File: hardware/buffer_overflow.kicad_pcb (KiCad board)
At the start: 2 copper layers, 33.1 x 29.9 mm, 20 parts, among them J1 E1, J2 E2, U1 LM741

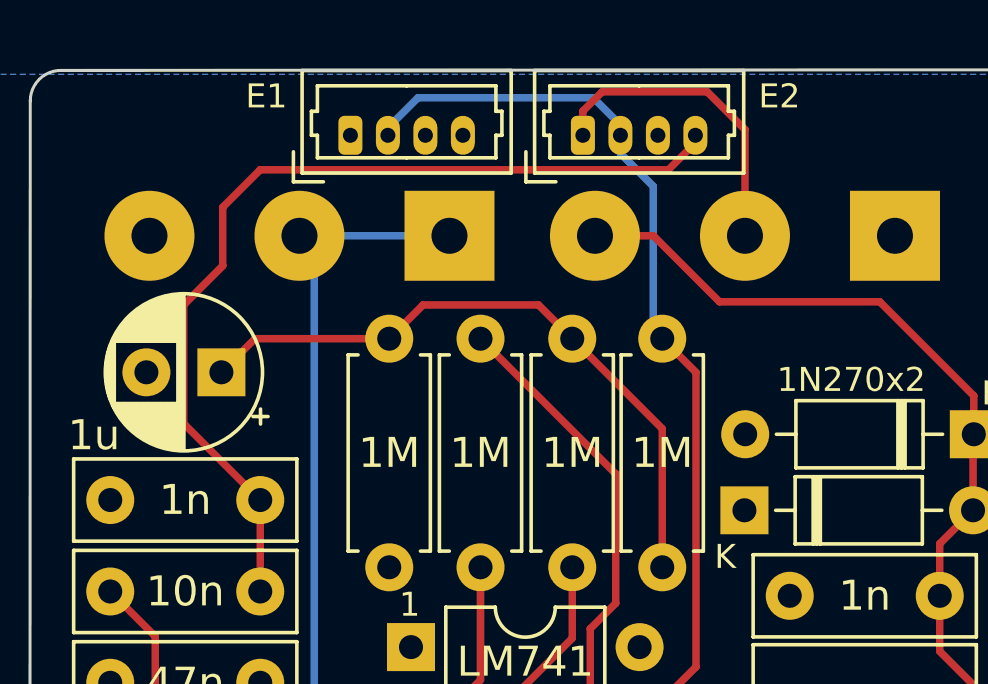
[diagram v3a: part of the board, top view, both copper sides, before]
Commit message: swap connectors to be on the same side as Noise Floor
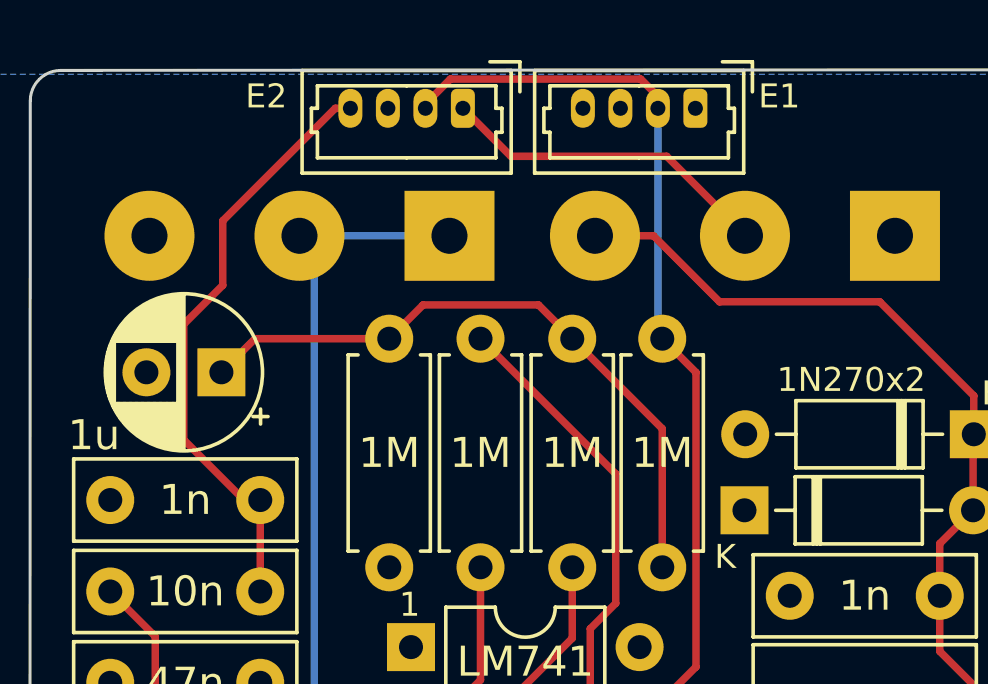
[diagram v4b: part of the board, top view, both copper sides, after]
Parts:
- moved J1 11.5 mm to (67.3, 29.2), turned to 180 degrees
- moved J2 4.10 mm to (59.6, 29.2), turned to 180 degrees
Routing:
- net /EFFECT_IN: track 31.3 -> 20.1 mm
- net /EFFECT_OUT: track 10.5 -> 11.2 mm
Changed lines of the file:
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@@
     (title "Buffer Overflow Drive Effect")
     (date "2023-03-03")
-    (rev "v0.36")
+    (rev "v0.37")
     (comment 1 " github.com/whbeers/buffer_overflow")
   )
@@
   )
   (footprint "Connector_Molex:Molex_PicoBlade_53047-0410_1x04_P1.25mm_Vertical" (layer "F.Cu")
-    (at 55.805112 30.1)
+    (at 67.305113 29.199999 180)
     (descr "Molex PicoBlade Connector System, 53047-0410, 4 Pins per row (http://www.molex.com/pdm_docs/sd/530470610_sd.pdf), generated with kicad-footprint-generator")
     (tags "connector Molex PicoBlade side entry")
@@
         (effects (font (size 1 1) (thickness 0.15)))
     )
-    (fp_text value "E1" (at -2.8 -1.3) (layer "F.SilkS" knockout)
+    (fp_text value "E1" (at -2.794887 0.399999) (layer "F.SilkS" knockout)
         (effects (font (size 0.8 0.8) (thickness 0.15)))
     )
@@
     (fp_line (start 5.25 1.15) (end 5.25 -2.05)
       (stroke (width 0.1) (type solid)) (layer "F.Fab"))
-    (pad "1" thru_hole roundrect (at 0 0) (size 0.8 1.3) (drill 0.5) (layers "*.Cu" "*.Mask") (roundrect_rratio 0.25)
+    (pad "1" thru_hole roundrect (at 0 0 180) (size 0.8 1.3) (drill 0.5) (layers "*.Cu" "*.Mask") (roundrect_rratio 0.25)
       (net 12 "unconnected-(J1-Pin_1-Pad1)") (pinfunction "Pin_1") (pintype "passive+no_connect"))
-    (pad "2" thru_hole oval (at 1.25 0) (size 0.8 1.3) (drill 0.5) (layers "*.Cu" "*.Mask")
+    (pad "2" thru_hole oval (at 1.25 0 180) (size 0.8 1.3) (drill 0.5) (layers "*.Cu" "*.Mask")
       (net 13 "/9V0") (pinfunction "Pin_2") (pintype "passive"))
-    (pad "3" thru_hole oval (at 2.5 0) (size 0.8 1.3) (drill 0.5) (layers "*.Cu" "*.Mask")
+    (pad "3" thru_hole oval (at 2.5 0 180) (size 0.8 1.3) (drill 0.5) (layers "*.Cu" "*.Mask")
       (net 14 "unconnected-(J1-Pin_3-Pad3)") (pinfunction "Pin_3") (pintype "passive+no_connect"))
-    (pad "4" thru_hole oval (at 3.75 0) (size 0.8 1.3) (drill 0.5) (layers "*.Cu" "*.Mask")
+    (pad "4" thru_hole oval (at 3.75 0 180) (size 0.8 1.3) (drill 0.5) (layers "*.Cu" "*.Mask")
       (net 15 "unconnected-(J1-Pin_4-Pad4)") (pinfunction "Pin_4") (pintype "passive+no_connect"))
     (model "${KICAD6_3DMODEL_DIR}/Connector_Molex.3dshapes/Molex_PicoBlade_53047-0410_1x04_P1.25mm_Vertical.wrl"
@@
   )
   (footprint "Connector_Molex:Molex_PicoBlade_53047-0410_1x04_P1.25mm_Vertical" (layer "F.Cu")
-    (at 63.555112 30.1)
+    (at 59.555113 29.199999 180)
     (descr "Molex PicoBlade Connector System, 53047-0410, 4 Pins per row (http://www.molex.com/pdm_docs/sd/530470610_sd.pdf), generated with kicad-footprint-generator")
     (tags "connector Molex PicoBlade side entry")
@@
         (effects (font (size 1 1) (thickness 0.15)))
     )
-    (fp_text value "E2" (at 6.55 -1.3) (layer "F.SilkS" knockout)
+    (fp_text value "E2" (at 6.555113 0.399999) (layer "F.SilkS" knockout)
         (effects (font (size 0.8 0.8) (thickness 0.15)))
     )
@@
     (fp_line (start 5.25 1.15) (end 5.25 -2.05)
       (stroke (width 0.1) (type solid)) (layer "F.Fab"))
-    (pad "1" thru_hole roundrect (at 0 0) (size 0.8 1.3) (drill 0.5) (layers "*.Cu" "*.Mask") (roundrect_rratio 0.25)
+    (pad "1" thru_hole roundrect (at 0 0 180) (size 0.8 1.3) (drill 0.5) (layers "*.Cu" "*.Mask") (roundrect_rratio 0.25)
       (net 16 "/EFFECT_OUT") (pinfunction "Pin_1") (pintype "passive"))
-    (pad "2" thru_hole oval (at 1.25 0) (size 0.8 1.3) (drill 0.5) (layers "*.Cu" "*.Mask")
+    (pad "2" thru_hole oval (at 1.25 0 180) (size 0.8 1.3) (drill 0.5) (layers "*.Cu" "*.Mask")
       (net 13 "/9V0") (pinfunction "Pin_2") (pintype "passive"))
-    (pad "3" thru_hole oval (at 2.5 0) (size 0.8 1.3) (drill 0.5) (layers "*.Cu" "*.Mask")
+    (pad "3" thru_hole oval (at 2.5 0 180) (size 0.8 1.3) (drill 0.5) (layers "*.Cu" "*.Mask")
       (net 1 "GND") (pinfunction "Pin_3") (pintype "passive"))
-    (pad "4" thru_hole oval (at 3.75 0) (size 0.8 1.3) (drill 0.5) (layers "*.Cu" "*.Mask")
+    (pad "4" thru_hole oval (at 3.75 0 180) (size 0.8 1.3) (drill 0.5) (layers "*.Cu" "*.Mask")
       (net 5 "/EFFECT_IN") (pinfunction "Pin_4") (pintype "passive"))
     (model "${KICAD6_3DMODEL_DIR}/Connector_Molex.3dshapes/Molex_PicoBlade_53047-0410_1x04_P1.25mm_Vertical.wrl"
@@
   (segment (start 70.95 54.45) (end 75.45 49.95) (width 0.25) (layer "F.Cu") (net 4))
   (segment (start 68.99 54.45) (end 70.95 54.45) (width 0.25) (layer "F.Cu") (net 4))
-  (segment (start 67.305112 30.35) (end 66.405112 31.25) (width 0.25) (layer "F.Cu") (net 5))
-  (segment (start 52.8 31.25) (end 51.55 32.5) (width 0.25) (layer "F.Cu") (net 5))
-  (segment (start 50.25 39.708) (end 52.8 42.258) (width 0.25) (layer "F.Cu") (net 5))
+  (segment (start 51.55 32.95) (end 51.55 35.1) (width 0.25) (layer "F.Cu") (net 5))
+  (segment (start 50.25 36.4) (end 50.25 40.25) (width 0.25) (layer "F.Cu") (net 5))
+  (segment (start 55.805113 29.199999) (end 55.300001 29.199999) (width 0.25) (layer "F.Cu") (net 5))
   (segment (start 52.8 42.258) (end 52.8 45.306) (width 0.25) (layer "F.Cu") (net 5))
-  (segment (start 66.405112 31.25) (end 52.8 31.25) (width 0.25) (layer "F.Cu") (net 5))
-  (segment (start 51.55 34.45) (end 50.25 35.75) (width 0.25) (layer "F.Cu") (net 5))
-  (segment (start 51.55 32.5) (end 51.55 34.45) (width 0.25) (layer "F.Cu") (net 5))
-  (segment (start 50.25 35.75) (end 50.25 39.708) (width 0.25) (layer "F.Cu") (net 5))
-  (segment (start 67.305112 30.1) (end 67.305112 30.35) (width 0.25) (layer "F.Cu") (net 5))
+  (segment (start 51.55 35.1) (end 50.25 36.4) (width 0.25) (layer "F.Cu") (net 5))
+  (segment (start 55.300001 29.199999) (end 51.55 32.95) (width 0.25) (layer "F.Cu") (net 5))
+  (segment (start 50.25 40.25) (end 52.258 42.258) (width 0.25) (layer "F.Cu") (net 5))
+  (segment (start 52.258 42.258) (end 52.8 42.258) (width 0.25) (layer "F.Cu") (net 5))
   (segment (start 46.69 54.448) (end 49.3 51.838) (width 0.25) (layer "F.Cu") (net 6))
   (segment (start 49.3 51.838) (end 49.3 46.806) (width 0.25) (layer "F.Cu") (net 6))
@@
   (segment (start 67.325 38.005) (end 67.325 47.82) (width 0.25) (layer "F.Cu") (net 13))
   (segment (start 67.325 47.82) (end 65.445 49.7) (width 0.25) (layer "F.Cu") (net 13))
+  (segment (start 66.055113 28.799999) (end 65.480113 28.224999) (width 0.25) (layer "F.Cu") (net 13))
+  (segment (start 65.480113 28.224999) (end 59.137651 28.224999) (width 0.25) (layer "F.Cu") (net 13))
+  (segment (start 66.055113 29.199999) (end 66.055113 28.799999) (width 0.25) (layer "F.Cu") (net 13))
+  (segment (start 59.137651 28.224999) (end 58.305113 29.057537) (width 0.25) (layer "F.Cu") (net 13))
+  (segment (start 58.305113 29.057537) (end 58.305113 29.199999) (width 0.25) (layer "F.Cu") (net 13))
   (segment (start 66.2 36.88) (end 67.325 38.005) (width 0.25) (layer "F.Cu") (net 13))
-  (segment (start 58.055112 28.85) (end 57.055112 29.85) (width 0.25) (layer "B.Cu") (net 13))
-  (segment (start 64.805112 30.1) (end 64.805112 29.755112) (width 0.25) (layer "B.Cu") (net 13))
-  (segment (start 64.805112 29.755112) (end 63.9 28.85) (width 0.25) (layer "B.Cu") (net 13))
-  (segment (start 57.05 30.3) (end 57.05 29.8) (width 0.25) (layer "B.Cu") (net 13))
-  (segment (start 65.9 31.8) (end 64.805112 30.705112) (width 0.25) (layer "B.Cu") (net 13))
-  (segment (start 65.9 36.58) (end 65.9 31.8) (width 0.25) (layer "B.Cu") (net 13))
-  (segment (start 66.2 36.88) (end 65.9 36.58) (width 0.25) (layer "B.Cu") (net 13))
-  (segment (start 57.055112 29.85) (end 57.055112 30.1) (width 0.25) (layer "B.Cu") (net 13))
-  (segment (start 63.9 28.85) (end 58.055112 28.85) (width 0.25) (layer "B.Cu") (net 13))
-  (segment (start 64.805112 30.705112) (end 64.805112 30.1) (width 0.25) (layer "B.Cu") (net 13))
-  (segment (start 63.555112 29.294888) (end 63.555112 30.1) (width 0.25) (layer "F.Cu") (net 16))
-  (segment (start 68.9575 29.9075) (end 67.7 28.65) (width 0.25) (layer "F.Cu") (net 16))
-  (segment (start 68.9575 33.45) (end 68.9575 29.9075) (width 0.25) (layer "F.Cu") (net 16))
-  (segment (start 64.2 28.65) (end 63.555112 29.294888) (width 0.25) (layer "F.Cu") (net 16))
-  (segment (start 67.7 28.65) (end 64.2 28.65) (width 0.25) (layer "F.Cu") (net 16))
+  (segment (start 66.055113 29.199999) (end 66.055113 36.735113) (width 0.25) (layer "B.Cu") (net 13))
+  (segment (start 66.055113 36.735113) (end 66.2 36.88) (width 0.25) (layer "B.Cu") (net 13))
+  (segment (start 61.155114 30.8) (end 59.555113 29.199999) (width 0.25) (layer "F.Cu") (net 16))
+  (segment (start 66.35 30.8) (end 61.155114 30.8) (width 0.25) (layer "F.Cu") (net 16))
+  (segment (start 68.9575 33.45) (end 68.9575 33.4075) (width 0.25) (layer "F.Cu") (net 16))
+  (segment (start 68.9575 33.4075) (end 66.35 30.8) (width 0.25) (layer "F.Cu") (net 16))
   (zone (net 1) (net_name "GND") (layer "B.Cu") (hatch edge 0.5)
     (connect_pads yes (clearance 0.508))
@@
         (xy 42.545 28.067)
       )
-    )
-  )
-  (group "" (id 44640d10-d8b0-4d10-8120-2862c2ace293)
-    (members
-      2863f98b-8943-4d5b-a6a4-d4917c9955a0
-      e8f1f366-1300-4382-9eb1-e7ea8b674607
     )
   )
@@
     (members
       e10283d1-a943-448b-b704-b4369c76185f
-      e59c07ca-e828-485d-8df7-598f3e4653e9
     )
   )
@@
     )
   )
+  (group "" (id 44640d10-d8b0-4d10-8120-2862c2ace293)
+    (members
+      2863f98b-8943-4d5b-a6a4-d4917c9955a0
+      3fd1133f-6a15-453f-9955-076d7ddada48
+      58ac90e8-e3b5-4925-9eaf-6aa123984e52
+      695f64c0-f4cf-4480-8a71-49eea9fb64d9
+      a26313fd-cb98-48cc-a445-f2466f3eeba6
+      af7734d1-66ab-49d0-ae24-1201dfe3ad5b
+      beb3796a-b8f2-4311-8699-af5658786aba
+      bf1f60d0-b900-4a9c-ae57-c94d054c15dd
+      d71d6460-fbc3-441c-965b-82b468e7d0f1
+      e8f1f366-1300-4382-9eb1-e7ea8b674607
+      e989a740-62a0-4e95-a4c7-73adee2570a0
+      eab2ae7c-9b4e-4f0e-9e92-98b32670b376
+      fd5ebd50-ebef-48b8-9dc5-55969baaa9df
+    )
+  )

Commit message: condense to a single connector, bump rev to v0.38
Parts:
- removed the J1 at (67.3, 29.2)
- J1: renamed from J2; value E2 -> E1
- moved J1 3.82 mm to (63.4, 29.2)
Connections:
- net VREF renamed /VREF
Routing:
- net /9V0: track 30.7 -> 24.7 mm
- net /EFFECT_OUT: track 11.2 -> 7.32 mm
- net /EFFECT_IN: track 20.1 -> 23.9 mm
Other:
- board size 33.1 x 29.9 mm -> 33.1 x 30.1 mm
- board text added: "${COMMENT1} ${REVISION}"
- board text removed: "${COMMENT1}"
- board text removed: "${REVISION}"
